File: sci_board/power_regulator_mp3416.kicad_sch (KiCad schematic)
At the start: 5 parts, among them U13 TPS631000DRLR

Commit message: clenup BOM for SCI and AUX
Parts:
- R161: Note Regulator -> regulator; Part Number RT0402BRD0791KL -> RC0402FR-0791KL; Tolerance 0.1 -> 1
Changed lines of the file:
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@@
 			)
 		)
-		(property "Description" ""
+		(property "Description" "Non-Isolated PoL Module DC DC Converter 1 Output 1.2 ~ 5.3V 2A 1.6V - 5.5V Input"
 			(at 72.39 132.08 0)
 			(effects
@@
 		)
 		(property "Note" ""
-			(at 72.39 132.08 0)
-			(effects
-				(font
-					(size 1.27 1.27)
-				)
-				(hide yes)
-			)
-		)
-		(property "MANUFACTURER" ""
-			(at 72.39 132.08 0)
-			(effects
-				(font
-					(size 1.27 1.27)
-				)
-				(hide yes)
-			)
-		)
-		(property "MAXIMUM_PACKAGE_HEIGHT" ""
-			(at 72.39 132.08 0)
-			(effects
-				(font
-					(size 1.27 1.27)
-				)
-				(hide yes)
-			)
-		)
-		(property "Manufactorer" ""
-			(at 72.39 132.08 0)
-			(effects
-				(font
-					(size 1.27 1.27)
-				)
-				(hide yes)
-			)
-		)
-		(property "PARTREV" ""
-			(at 72.39 132.08 0)
-			(effects
-				(font
-					(size 1.27 1.27)
-				)
-				(hide yes)
-			)
-		)
-		(property "STANDARD" ""
 			(at 72.39 132.08 0)
 			(effects
@@
 			)
 		)
-		(property "Description" "Resistor, small symbol"
+		(property "Description" "Resistor"
 			(at 128.905 135.89 0)
 			(effects
@@
 			)
 		)
-		(property "Part Number" "RT0402BRD0791KL"
-			(at 128.905 135.89 0)
-			(effects
-				(font
-					(size 1.27 1.27)
-				)
-				(hide yes)
-			)
-		)
-		(property "Tolerance" "0.1"
-			(at 128.905 135.89 0)
-			(effects
-				(font
-					(size 1.27 1.27)
-				)
-				(hide yes)
-			)
-		)
-		(property "Note" "Regulator"
-			(at 128.905 135.89 0)
-			(effects
-				(font
-					(size 1.27 1.27)
-				)
-				(hide yes)
-			)
-		)
-		(property "MANUFACTURER" ""
-			(at 128.905 135.89 0)
-			(effects
-				(font
-					(size 1.27 1.27)
-				)
-				(hide yes)
-			)
-		)
-		(property "MAXIMUM_PACKAGE_HEIGHT" ""
-			(at 128.905 135.89 0)
-			(effects
-				(font
-					(size 1.27 1.27)
-				)
-				(hide yes)
-			)
-		)
-		(property "Manufactorer" ""
-			(at 128.905 135.89 0)
-			(effects
-				(font
-					(size 1.27 1.27)
-				)
-				(hide yes)
-			)
-		)
-		(property "PARTREV" ""
-			(at 128.905 135.89 0)
-			(effects
-				(font
-					(size 1.27 1.27)
-				)
-				(hide yes)
-			)
-		)
-		(property "STANDARD" ""
+		(property "Part Number" "RC0402FR-0791KL "
+			(at 128.905 135.89 0)
+			(effects
+				(font
+					(size 1.27 1.27)
+				)
+				(hide yes)
+			)
+		)
+		(property "Tolerance" "1"
+			(at 128.905 135.89 0)
+			(effects
+				(font
+					(size 1.27 1.27)
+				)
+				(hide yes)
+			)
+		)
+		(property "Note" "regulator"
 			(at 128.905 135.89 0)
 			(effects
@@
 			(project "sci_board"
 				(path "/b4b2c88d-f6cd-4e60-862d-e21f68728580/5e5b27f8-7a4c-45d0-95f8-aff71797fcd3/2f5a2990-2dc0-472a-952a-1bfd830a3aba"
-					(reference "R45")
+					(reference "R46")
 					(unit 1)
 				)
@@
 		)
 		(property "Note" ""
-			(at 72.39 143.51 0)
-			(effects
-				(font
-					(size 1.27 1.27)
-				)
-				(hide yes)
-			)
-		)
-		(property "MANUFACTURER" ""
-			(at 72.39 143.51 0)
-			(effects
-				(font
-					(size 1.27 1.27)
-				)
-				(hide yes)
-			)
-		)
-		(property "MAXIMUM_PACKAGE_HEIGHT" ""
-			(at 72.39 143.51 0)
-			(effects
-				(font
-					(size 1.27 1.27)
-				)
-				(hide yes)
-			)
-		)
-		(property "Manufactorer" ""
-			(at 72.39 143.51 0)
-			(effects
-				(font
-					(size 1.27 1.27)
-				)
-				(hide yes)
-			)
-		)
-		(property "PARTREV" ""
-			(at 72.39 143.51 0)
-			(effects
-				(font
-					(size 1.27 1.27)
-				)
-				(hide yes)
-			)
-		)
-		(property "STANDARD" ""
 			(at 72.39 143.51 0)
 			(effects
@@
 			)
 		)
-		(property "MANUFACTURER" ""
-			(at 49.53 139.7 0)
-			(effects
-				(font
-					(size 1.27 1.27)
-				)
-				(hide yes)
-			)
-		)
-		(property "MAXIMUM_PACKAGE_HEIGHT" ""
-			(at 49.53 139.7 0)
-			(effects
-				(font
-					(size 1.27 1.27)
-				)
-				(hide yes)
-			)
-		)
-		(property "Manufactorer" ""
-			(at 49.53 139.7 0)
-			(effects
-				(font
-					(size 1.27 1.27)
-				)
-				(hide yes)
-			)
-		)
-		(property "PARTREV" ""
-			(at 49.53 139.7 0)
-			(effects
-				(font
-					(size 1.27 1.27)
-				)
-				(hide yes)
-			)
-		)
-		(property "STANDARD" ""
-			(at 49.53 139.7 0)
-			(effects
-				(font
-					(size 1.27 1.27)
-				)
-				(hide yes)
-			)
-		)
 		(pin "2"
 		)
@@
 			(at 59.69 139.7 0)
 			(effects
-				(font
-					(size 1.27 1.27)
-				)
-				(hide yes)
-			)
-		)
-		(property "MANUFACTURER" ""
-			(at 59.69 139.7 0)
-			(effects
-				(font
-					(size 1.27 1.27)
-				)
-				(hide yes)
-			)
-		)
-		(property "MAXIMUM_PACKAGE_HEIGHT" ""
-			(at 59.69 139.7 0)
-			(effects
-				(font
-					(size 1.27 1.27)
-				)
-				(hide yes)
-			)
-		)
-		(property "Manufactorer" ""
-			(at 59.69 139.7 0)
-			(effects
-				(font
-					(size 1.27 1.27)
-				)
-				(hide yes)
-			)
-		)
-		(property "PARTREV" ""
-			(at 59.69 139.7 0)
-			(effects
-				(font
-					(size 1.27 1.27)
-				)
-				(hide yes)
-			)
-		)
-		(property "STANDARD" ""
-			(at 59.69 139.7 0)
-			(effects

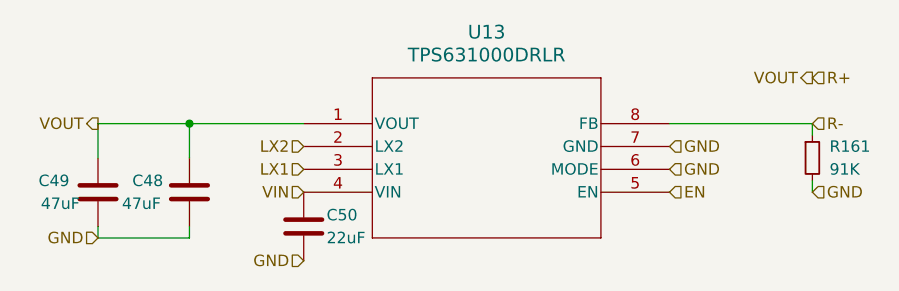
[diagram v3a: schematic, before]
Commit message: cleaning up bom: remove main camera port since it has not pullups and capacitors, correcting some errors in camera switch
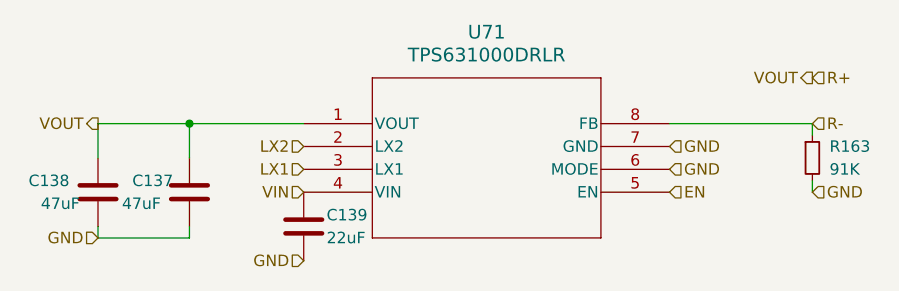
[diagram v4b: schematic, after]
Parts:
- renumbered C48 to C137, C49 to C138, C50 to C139, R161 to R163, U13 to U71

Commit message: QC, add second 3V regulator to AUX, INT pullups on AUX SCI AVI
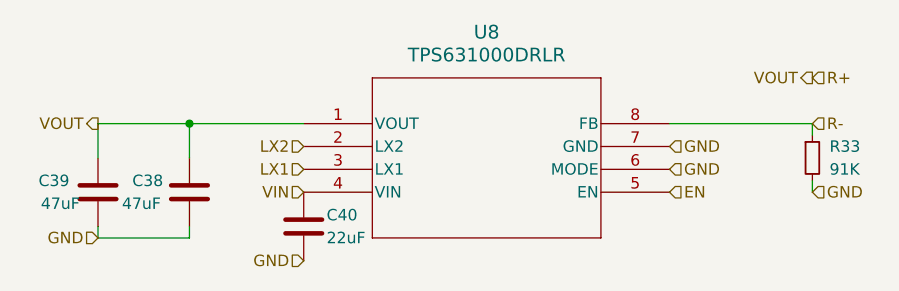
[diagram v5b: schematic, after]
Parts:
- renumbered C137 to C38, C138 to C39, C139 to C40, R163 to R33, U71 to U8
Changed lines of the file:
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@@
 		(dnp no)
 		(fields_autoplaced yes)
-		(property "Reference" "U71"
+		(property "Reference" "U8"
 			(at 92.71 121.92 0)
 			(effects
@@
 		)
 		(instances
-			(project ""
-				(path "/05170af6-30ef-4c3a-b972-f098085da1bc/87930429-600a-4d20-9691-47e157ed6d1e"
-					(reference "U71")
-					(unit 1)
-				)
-				(path "/05170af6-30ef-4c3a-b972-f098085da1bc/e1d2fe3b-9ba5-4366-9cc3-67e5d340cfc0/4b0ead8a-9397-4a83-9955-863b935c5b9c"
-					(reference "U8")
-					(unit 1)
-				)
-				(path "/05170af6-30ef-4c3a-b972-f098085da1bc/e1d2fe3b-9ba5-4366-9cc3-67e5d340cfc0/744250af-b7e3-4edd-bc04-e013bd519440"
-					(reference "U12")
-					(unit 1)
-				)
-				(path "/05170af6-30ef-4c3a-b972-f098085da1bc/e1d2fe3b-9ba5-4366-9cc3-67e5d340cfc0/772eb76d-f57b-4f14-8409-6548bfc340ef"
-					(reference "U11")
-					(unit 1)
-				)
-			)
 			(project "aux_board"
 				(path "/85134265-2435-454a-99c4-e49d8e69c5c2/180ab09f-8202-4a23-a970-ad767a3abcbf"
+					(reference "U8")
+					(unit 1)
+				)
+				(path "/85134265-2435-454a-99c4-e49d8e69c5c2/21705b31-e71e-4020-a43e-3303465bf5fd"
+					(reference "U6")
+					(unit 1)
+				)
+				(path "/85134265-2435-454a-99c4-e49d8e69c5c2/89862a4b-05be-454b-946e-6c4f5a4f01a7"
+					(reference "U9")
+					(unit 1)
+				)
+				(path "/85134265-2435-454a-99c4-e49d8e69c5c2/c6f75225-fda9-49b7-af41-6a3b5c80f9a2"
 					(reference "U7")
-					(unit 1)
-				)
-				(path "/85134265-2435-454a-99c4-e49d8e69c5c2/89862a4b-05be-454b-946e-6c4f5a4f01a7"
-					(reference "U6")
-					(unit 1)
-				)
-				(path "/85134265-2435-454a-99c4-e49d8e69c5c2/c6f75225-fda9-49b7-af41-6a3b5c80f9a2"
-					(reference "U8")
-					(unit 1)
-				)
-			)
-			(project "sci_board"
-				(path "/b4b2c88d-f6cd-4e60-862d-e21f68728580/5e5b27f8-7a4c-45d0-95f8-aff71797fcd3/2f5a2990-2dc0-472a-952a-1bfd830a3aba"
-					(reference "U28")
-					(unit 1)
-				)
-				(path "/b4b2c88d-f6cd-4e60-862d-e21f68728580/5e5b27f8-7a4c-45d0-95f8-aff71797fcd3/7fde3d19-3e51-4869-ba44-af6d0a67b762"
-					(reference "U27")
 					(unit 1)
 				)
@@
 		(on_board yes)
 		(dnp no)
-		(property "Reference" "R163"
+		(property "Reference" "R33"
 			(at 130.81 134.62 0)
 			(effects
@@
 		)
 		(instances
-			(project ""
-				(path "/05170af6-30ef-4c3a-b972-f098085da1bc/87930429-600a-4d20-9691-47e157ed6d1e"
-					(reference "R163")
-					(unit 1)
-				)
-				(path "/05170af6-30ef-4c3a-b972-f098085da1bc/e1d2fe3b-9ba5-4366-9cc3-67e5d340cfc0/4b0ead8a-9397-4a83-9955-863b935c5b9c"
-					(reference "R43")
-					(unit 1)
-				)
-				(path "/05170af6-30ef-4c3a-b972-f098085da1bc/e1d2fe3b-9ba5-4366-9cc3-67e5d340cfc0/744250af-b7e3-4edd-bc04-e013bd519440"
-					(reference "R49")
-					(unit 1)
-				)
-				(path "/05170af6-30ef-4c3a-b972-f098085da1bc/e1d2fe3b-9ba5-4366-9cc3-67e5d340cfc0/772eb76d-f57b-4f14-8409-6548bfc340ef"
-					(reference "R48")
-					(unit 1)
-				)
-			)
 			(project "aux_board"
 				(path "/85134265-2435-454a-99c4-e49d8e69c5c2/180ab09f-8202-4a23-a970-ad767a3abcbf"
-					(reference "R29")
+					(reference "R33")
+					(unit 1)
+				)
+				(path "/85134265-2435-454a-99c4-e49d8e69c5c2/21705b31-e71e-4020-a43e-3303465bf5fd"
+					(reference "R31")
 					(unit 1)
 				)
 				(path "/85134265-2435-454a-99c4-e49d8e69c5c2/89862a4b-05be-454b-946e-6c4f5a4f01a7"
-					(reference "R27")
+					(reference "R34")
 					(unit 1)
 				)
 				(path "/85134265-2435-454a-99c4-e49d8e69c5c2/c6f75225-fda9-49b7-af41-6a3b5c80f9a2"
-					(reference "R31")
-					(unit 1)
-				)
-			)
-			(project "sci_board"
-				(path "/b4b2c88d-f6cd-4e60-862d-e21f68728580/5e5b27f8-7a4c-45d0-95f8-aff71797fcd3/2f5a2990-2dc0-472a-952a-1bfd830a3aba"
-					(reference "R52")
-					(unit 1)
-				)
-				(path "/b4b2c88d-f6cd-4e60-862d-e21f68728580/5e5b27f8-7a4c-45d0-95f8-aff71797fcd3/7fde3d19-3e51-4869-ba44-af6d0a67b762"
-					(reference "R50")
+					(reference "R32")
 					(unit 1)
 				)
@@
 		(on_board yes)
 		(dnp no)
-		(property "Reference" "C139"
+		(property "Reference" "C40"
 			(at 74.93 142.24 0)
 			(effects
@@
 		)
 		(instances
-			(project ""
-				(path "/05170af6-30ef-4c3a-b972-f098085da1bc/87930429-600a-4d20-9691-47e157ed6d1e"
-					(reference "C139")
-					(unit 1)
-				)
-				(path "/05170af6-30ef-4c3a-b972-f098085da1bc/e1d2fe3b-9ba5-4366-9cc3-67e5d340cfc0/4b0ead8a-9397-4a83-9955-863b935c5b9c"
-					(reference "C33")
-					(unit 1)
-				)
-				(path "/05170af6-30ef-4c3a-b972-f098085da1bc/e1d2fe3b-9ba5-4366-9cc3-67e5d340cfc0/744250af-b7e3-4edd-bc04-e013bd519440"
-					(reference "C47")
-					(unit 1)
-				)
-				(path "/05170af6-30ef-4c3a-b972-f098085da1bc/e1d2fe3b-9ba5-4366-9cc3-67e5d340cfc0/772eb76d-f57b-4f14-8409-6548bfc340ef"
-					(reference "C44")
-					(unit 1)
-				)
-			)
 			(project "aux_board"
 				(path "/85134265-2435-454a-99c4-e49d8e69c5c2/180ab09f-8202-4a23-a970-ad767a3abcbf"
+					(reference "C40")
+					(unit 1)
+				)
+				(path "/85134265-2435-454a-99c4-e49d8e69c5c2/21705b31-e71e-4020-a43e-3303465bf5fd"
 					(reference "C34")
 					(unit 1)
 				)
 				(path "/85134265-2435-454a-99c4-e49d8e69c5c2/89862a4b-05be-454b-946e-6c4f5a4f01a7"
-					(reference "C31")
+					(reference "C43")
 					(unit 1)
 				)
 				(path "/85134265-2435-454a-99c4-e49d8e69c5c2/c6f75225-fda9-49b7-af41-6a3b5c80f9a2"
-					(reference "C38")
-					(unit 1)
-				)
-			)
-			(project "sci_board"
-				(path "/b4b2c88d-f6cd-4e60-862d-e21f68728580/5e5b27f8-7a4c-45d0-95f8-aff71797fcd3/2f5a2990-2dc0-472a-952a-1bfd830a3aba"
-					(reference "C66")
-					(unit 1)
-				)
-				(path "/b4b2c88d-f6cd-4e60-862d-e21f68728580/5e5b27f8-7a4c-45d0-95f8-aff71797fcd3/7fde3d19-3e51-4869-ba44-af6d0a67b762"
-					(reference "C62")
+					(reference "C37")
 					(unit 1)
 				)
@@
 		(on_board yes)
 		(dnp no)
-		(property "Reference" "C137"
+		(property "Reference" "C38"
 			(at 53.34 138.4299 0)
 			(effects
@@
 		)
 		(instances
-			(project ""
-				(path "/05170af6-30ef-4c3a-b972-f098085da1bc/87930429-600a-4d20-9691-47e157ed6d1e"
-					(reference "C137")
-					(unit 1)
-				)
-				(path "/05170af6-30ef-4c3a-b972-f098085da1bc/e1d2fe3b-9ba5-4366-9cc3-67e5d340cfc0/4b0ead8a-9397-4a83-9955-863b935c5b9c"
-					(reference "C31")
-					(unit 1)
-				)
-				(path "/05170af6-30ef-4c3a-b972-f098085da1bc/e1d2fe3b-9ba5-4366-9cc3-67e5d340cfc0/744250af-b7e3-4edd-bc04-e013bd519440"
-					(reference "C45")
-					(unit 1)
-				)
-				(path "/05170af6-30ef-4c3a-b972-f098085da1bc/e1d2fe3b-9ba5-4366-9cc3-67e5d340cfc0/772eb76d-f57b-4f14-8409-6548bfc340ef"
-					(reference "C42")
-					(unit 1)
-				)
-			)
 			(project "aux_board"
 				(path "/85134265-2435-454a-99c4-e49d8e69c5c2/180ab09f-8202-4a23-a970-ad767a3abcbf"
+					(reference "C38")
+					(unit 1)
+				)
+				(path "/85134265-2435-454a-99c4-e49d8e69c5c2/21705b31-e71e-4020-a43e-3303465bf5fd"
 					(reference "C32")
 					(unit 1)
 				)
 				(path "/85134265-2435-454a-99c4-e49d8e69c5c2/89862a4b-05be-454b-946e-6c4f5a4f01a7"
-					(reference "C29")
+					(reference "C41")
 					(unit 1)
 				)
 				(path "/85134265-2435-454a-99c4-e49d8e69c5c2/c6f75225-fda9-49b7-af41-6a3b5c80f9a2"
-					(reference "C36")
-					(unit 1)
-				)
-			)
-			(project "sci_board"
-				(path "/b4b2c88d-f6cd-4e60-862d-e21f68728580/5e5b27f8-7a4c-45d0-95f8-aff71797fcd3/2f5a2990-2dc0-472a-952a-1bfd830a3aba"
-					(reference "C64")
-					(unit 1)
-				)
-				(path "/b4b2c88d-f6cd-4e60-862d-e21f68728580/5e5b27f8-7a4c-45d0-95f8-aff71797fcd3/7fde3d19-3e51-4869-ba44-af6d0a67b762"
-					(reference "C60")
+					(reference "C35")
 					(unit 1)
 				)
@@
 		(on_board yes)
 		(dnp no)
-		(property "Reference" "C138"
+		(property "Reference" "C39"
 			(at 46.355 138.43 0)
 			(effects
@@
 		)
 		(instances
-			(project ""
-				(path "/05170af6-30ef-4c3a-b972-f098085da1bc/87930429-600a-4d20-9691-47e157ed6d1e"
-					(reference "C138")
-					(unit 1)
-				)
-				(path "/05170af6-30ef-4c3a-b972-f098085da1bc/e1d2fe3b-9ba5-4366-9cc3-67e5d340cfc0/4b0ead8a-9397-4a83-9955-863b935c5b9c"
-					(reference "C32")
-					(unit 1)
-				)
-				(path "/05170af6-30ef-4c3a-b972-f098085da1bc/e1d2fe3b-9ba5-4366-9cc3-67e5d340cfc0/744250af-b7e3-4edd-bc04-e013bd519440"
-					(reference "C46")
-					(unit 1)
-				)
-				(path "/05170af6-30ef-4c3a-b972-f098085da1bc/e1d2fe3b-9ba5-4366-9cc3-67e5d340cfc0/772eb76d-f57b-4f14-8409-6548bfc340ef"
-					(reference "C43")
-					(unit 1)
-				)
-			)
 			(project "aux_board"
 				(path "/85134265-2435-454a-99c4-e49d8e69c5c2/180ab09f-8202-4a23-a970-ad767a3abcbf"
+					(reference "C39")
+					(unit 1)
+				)
+				(path "/85134265-2435-454a-99c4-e49d8e69c5c2/21705b31-e71e-4020-a43e-3303465bf5fd"
 					(reference "C33")
 					(unit 1)
 				)
 				(path "/85134265-2435-454a-99c4-e49d8e69c5c2/89862a4b-05be-454b-946e-6c4f5a4f01a7"
-					(reference "C30")
+					(reference "C42")
 					(unit 1)
 				)
 				(path "/85134265-2435-454a-99c4-e49d8e69c5c2/c6f75225-fda9-49b7-af41-6a3b5c80f9a2"
-					(reference "C37")
-					(unit 1)
-				)
-			)
-			(project "sci_board"
-				(path "/b4b2c88d-f6cd-4e60-862d-e21f68728580/5e5b27f8-7a4c-45d0-95f8-aff71797fcd3/2f5a2990-2dc0-472a-952a-1bfd830a3aba"
-					(reference "C65")
-					(unit 1)
-				)
-				(path "/b4b2c88d-f6cd-4e60-862d-e21f68728580/5e5b27f8-7a4c-45d0-95f8-aff71797fcd3/7fde3d19-3e51-4869-ba44-af6d0a67b762"
-					(reference "C61")
-					(unit 1)
-				)
+					(reference "C36")
+					(unit 1)
+				)

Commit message: propate the changes to RF
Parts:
- renumbered C38 to C31, C39 to C32, C40 to C33, R33 to R43

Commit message: tweaks before merge
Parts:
- renumbered C31 to C137, C32 to C138, C33 to C139, R43 to R163, U8 to U71
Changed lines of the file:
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@@
 		(dnp no)
 		(fields_autoplaced yes)
-		(property "Reference" "U8"
+		(property "Reference" "U71"
 			(at 92.71 121.92 0)
 			(effects
@@
 		)
 		(property "Note" ""
+			(at 72.39 132.08 0)
+			(effects
+				(font
+					(size 1.27 1.27)
+				)
+				(hide yes)
+			)
+		)
+		(property "MANUFACTURER" ""
+			(at 72.39 132.08 0)
+			(effects
+				(font
+					(size 1.27 1.27)
+				)
+				(hide yes)
+			)
+		)
+		(property "MAXIMUM_PACKAGE_HEIGHT" ""
+			(at 72.39 132.08 0)
+			(effects
+				(font
+					(size 1.27 1.27)
+				)
+				(hide yes)
+			)
+		)
+		(property "PARTREV" ""
+			(at 72.39 132.08 0)
+			(effects
+				(font
+					(size 1.27 1.27)
+				)
+				(hide yes)
+			)
+		)
+		(property "STANDARD" ""
 			(at 72.39 132.08 0)
 			(effects
@@
 			(project "sci_board"
 				(path "/b4b2c88d-f6cd-4e60-862d-e21f68728580/5e5b27f8-7a4c-45d0-95f8-aff71797fcd3/2f5a2990-2dc0-472a-952a-1bfd830a3aba"
-					(reference "U?")
+					(reference "U28")
 					(unit 1)
 				)
 				(path "/b4b2c88d-f6cd-4e60-862d-e21f68728580/5e5b27f8-7a4c-45d0-95f8-aff71797fcd3/7fde3d19-3e51-4869-ba44-af6d0a67b762"
-					(reference "U?")
+					(reference "U27")
 					(unit 1)
 				)
@@
 		(on_board yes)
 		(dnp no)
-		(property "Reference" "R43"
+		(property "Reference" "R163"
 			(at 130.81 134.62 0)
 			(effects
@@
 		)
 		(property "Note" "regulator"
+			(at 128.905 135.89 0)
+			(effects
+				(font
+					(size 1.27 1.27)
+				)
+				(hide yes)
+			)
+		)
+		(property "MANUFACTURER" ""
+			(at 128.905 135.89 0)
+			(effects
+				(font
+					(size 1.27 1.27)
+				)
+				(hide yes)
+			)
+		)
+		(property "MAXIMUM_PACKAGE_HEIGHT" ""
+			(at 128.905 135.89 0)
+			(effects
+				(font
+					(size 1.27 1.27)
+				)
+				(hide yes)
+			)
+		)
+		(property "PARTREV" ""
+			(at 128.905 135.89 0)
+			(effects
+				(font
+					(size 1.27 1.27)
+				)
+				(hide yes)
+			)
+		)
+		(property "STANDARD" ""
 			(at 128.905 135.89 0)
 			(effects
@@
 			(project "sci_board"
 				(path "/b4b2c88d-f6cd-4e60-862d-e21f68728580/5e5b27f8-7a4c-45d0-95f8-aff71797fcd3/2f5a2990-2dc0-472a-952a-1bfd830a3aba"
-					(reference "R?")
+					(reference "R52")
 					(unit 1)
 				)
 				(path "/b4b2c88d-f6cd-4e60-862d-e21f68728580/5e5b27f8-7a4c-45d0-95f8-aff71797fcd3/7fde3d19-3e51-4869-ba44-af6d0a67b762"
-					(reference "R?")
+					(reference "R50")
 					(unit 1)
 				)
@@
 		(on_board yes)
 		(dnp no)
-		(property "Reference" "C33"
+		(property "Reference" "C139"
 			(at 74.93 142.24 0)
 			(effects
@@
 		)
 		(property "Note" ""
+			(at 72.39 143.51 0)
+			(effects
+				(font
+					(size 1.27 1.27)
+				)
+				(hide yes)
+			)
+		)
+		(property "MANUFACTURER" ""
+			(at 72.39 143.51 0)
+			(effects
+				(font
+					(size 1.27 1.27)
+				)
+				(hide yes)
+			)
+		)
+		(property "MAXIMUM_PACKAGE_HEIGHT" ""
+			(at 72.39 143.51 0)
+			(effects
+				(font
+					(size 1.27 1.27)
+				)
+				(hide yes)
+			)
+		)
+		(property "PARTREV" ""
+			(at 72.39 143.51 0)
+			(effects
+				(font
+					(size 1.27 1.27)
+				)
+				(hide yes)
+			)
+		)
+		(property "STANDARD" ""
 			(at 72.39 143.51 0)
 			(effects
@@
 			(project "sci_board"
 				(path "/b4b2c88d-f6cd-4e60-862d-e21f68728580/5e5b27f8-7a4c-45d0-95f8-aff71797fcd3/2f5a2990-2dc0-472a-952a-1bfd830a3aba"
-					(reference "C?")
+					(reference "C66")
 					(unit 1)
 				)
 				(path "/b4b2c88d-f6cd-4e60-862d-e21f68728580/5e5b27f8-7a4c-45d0-95f8-aff71797fcd3/7fde3d19-3e51-4869-ba44-af6d0a67b762"
-					(reference "C?")
+					(reference "C62")
 					(unit 1)
 				)
@@
 		(on_board yes)
 		(dnp no)
-		(property "Reference" "C31"
+		(property "Reference" "C137"
 			(at 53.34 138.4299 0)
 			(effects
@@
 		)
 		(property "Note" ""
+			(at 49.53 139.7 0)
+			(effects
+				(font
+					(size 1.27 1.27)
+				)
+				(hide yes)
+			)
+		)
+		(property "MANUFACTURER" ""
+			(at 49.53 139.7 0)
+			(effects
+				(font
+					(size 1.27 1.27)
+				)
+				(hide yes)
+			)
+		)
+		(property "MAXIMUM_PACKAGE_HEIGHT" ""
+			(at 49.53 139.7 0)
+			(effects
+				(font
+					(size 1.27 1.27)
+				)
+				(hide yes)
+			)
+		)
+		(property "PARTREV" ""
+			(at 49.53 139.7 0)
+			(effects
+				(font
+					(size 1.27 1.27)
+				)
+				(hide yes)
+			)
+		)
+		(property "STANDARD" ""
 			(at 49.53 139.7 0)
 			(effects
@@
 			(project "sci_board"
 				(path "/b4b2c88d-f6cd-4e60-862d-e21f68728580/5e5b27f8-7a4c-45d0-95f8-aff71797fcd3/2f5a2990-2dc0-472a-952a-1bfd830a3aba"
-					(reference "C?")
+					(reference "C64")
 					(unit 1)
 				)
 				(path "/b4b2c88d-f6cd-4e60-862d-e21f68728580/5e5b27f8-7a4c-45d0-95f8-aff71797fcd3/7fde3d19-3e51-4869-ba44-af6d0a67b762"
-					(reference "C?")
+					(reference "C60")
 					(unit 1)
 				)
@@
 		(on_board yes)
 		(dnp no)
-		(property "Reference" "C32"
+		(property "Reference" "C138"
 			(at 46.355 138.43 0)
 			(effects
@@
 		)
 		(property "Note" ""
+			(at 59.69 139.7 0)
+			(effects
+				(font
+					(size 1.27 1.27)
+				)
+				(hide yes)
+			)
+		)
+		(property "MANUFACTURER" ""
+			(at 59.69 139.7 0)
+			(effects
+				(font
+					(size 1.27 1.27)
+				)
+				(hide yes)
+			)
+		)
+		(property "MAXIMUM_PACKAGE_HEIGHT" ""
+			(at 59.69 139.7 0)
+			(effects
+				(font
+					(size 1.27 1.27)
+				)
+				(hide yes)
+			)
+		)
+		(property "PARTREV" ""
+			(at 59.69 139.7 0)
+			(effects
+				(font
+					(size 1.27 1.27)
+				)
+				(hide yes)
+			)
+		)
+		(property "STANDARD" ""
 			(at 59.69 139.7 0)
 			(effects
@@
 			(project "sci_board"
 				(path "/b4b2c88d-f6cd-4e60-862d-e21f68728580/5e5b27f8-7a4c-45d0-95f8-aff71797fcd3/2f5a2990-2dc0-472a-952a-1bfd830a3aba"
-					(reference "C?")
+					(reference "C65")
 					(unit 1)
 				)
 				(path "/b4b2c88d-f6cd-4e60-862d-e21f68728580/5e5b27f8-7a4c-45d0-95f8-aff71797fcd3/7fde3d19-3e51-4869-ba44-af6d0a67b762"
-					(reference "C?")
-					(unit 1)
-				)
+					(reference "C61")
+					(unit 1)
+				)
